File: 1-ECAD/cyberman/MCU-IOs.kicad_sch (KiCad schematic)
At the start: 17 parts, among them U1 ESP32-S3R16V, U15 W25Q128JWPIQ, U16 1054500101, X1 40 MHz

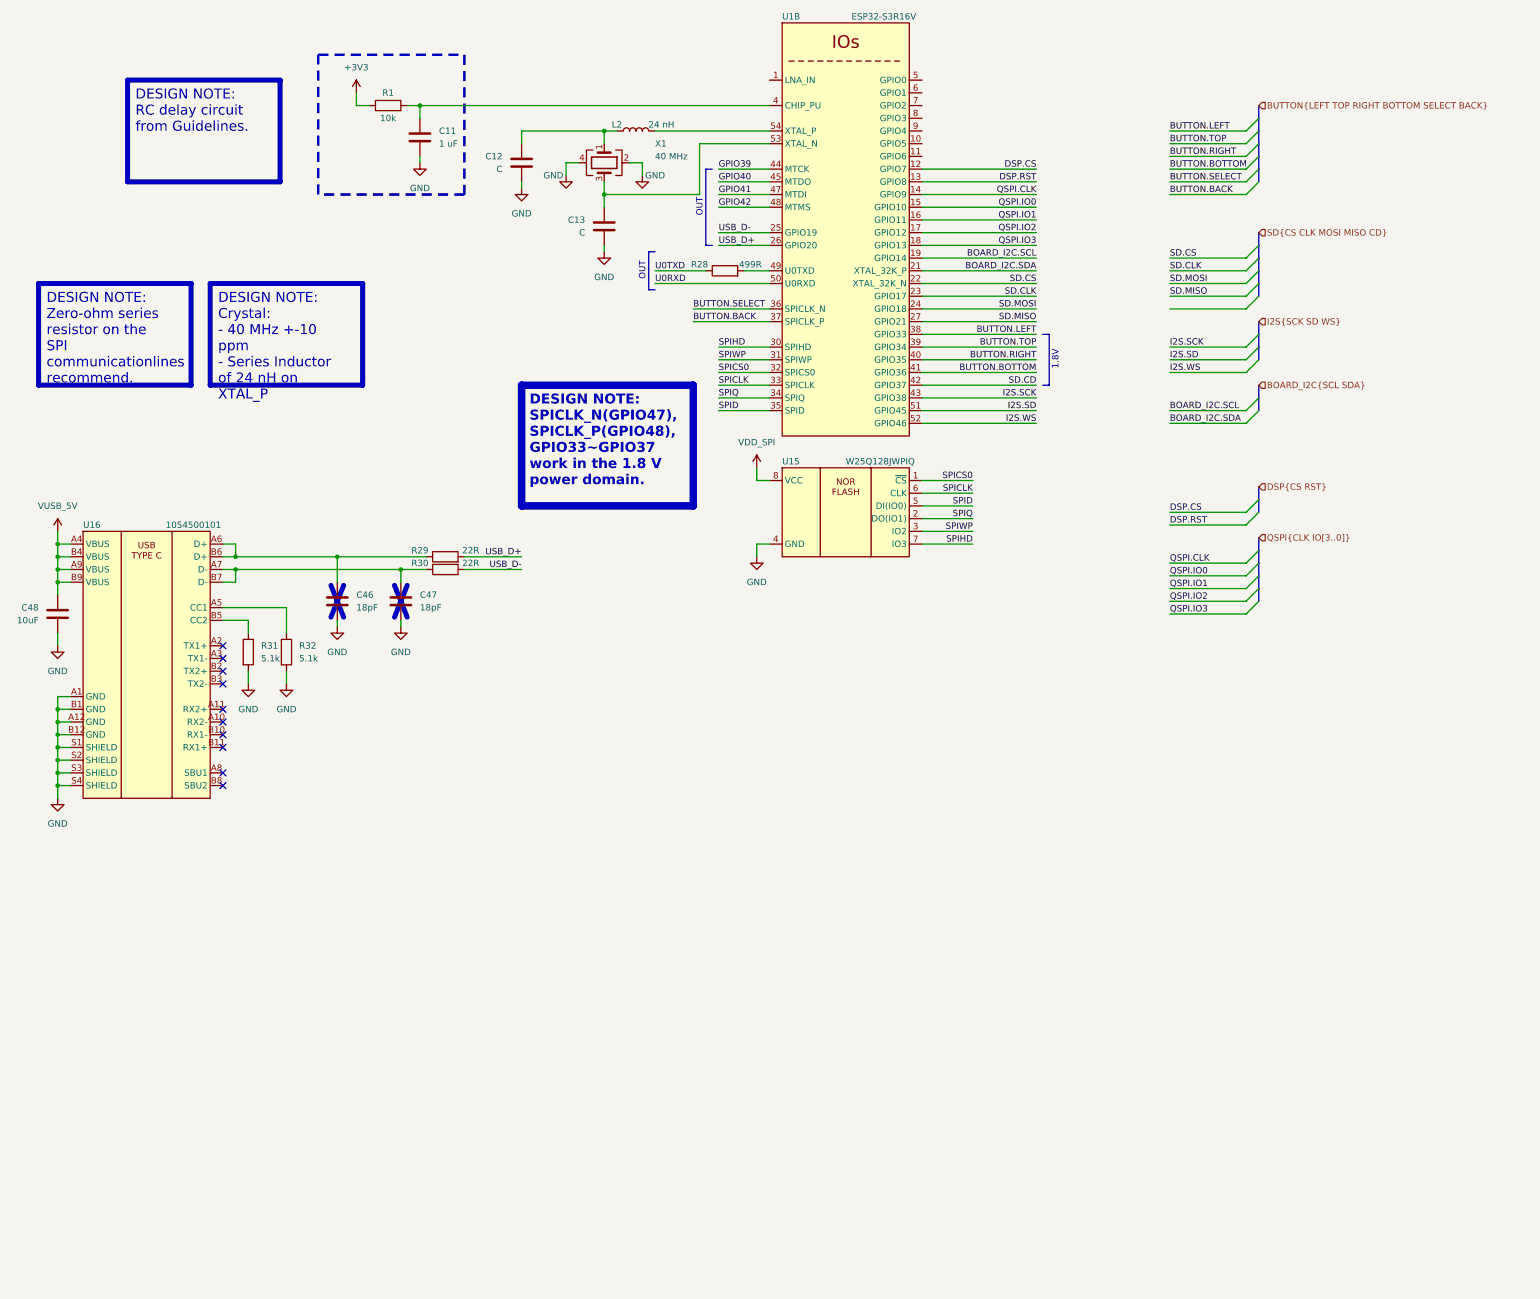
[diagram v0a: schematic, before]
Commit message: add expander io and pic
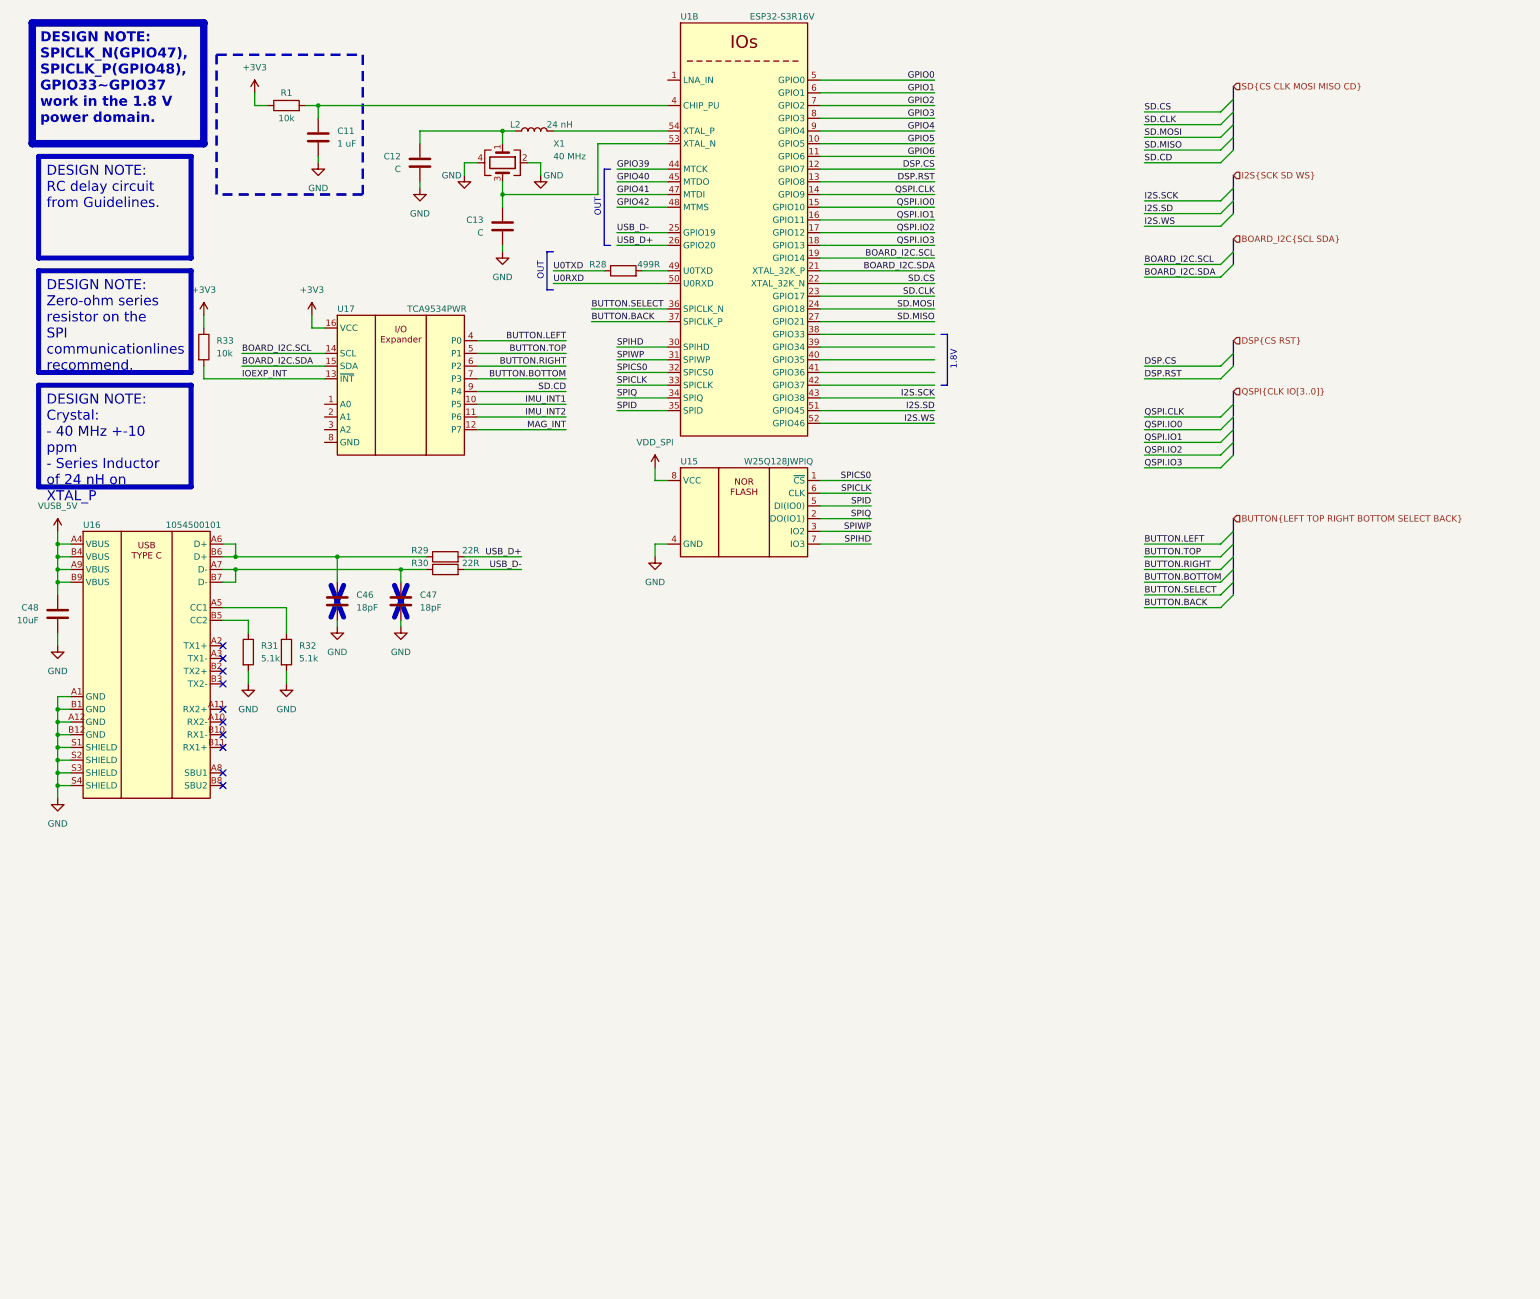
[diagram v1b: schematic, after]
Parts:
- added R33: 10k, symbol Device:R
- added U17: TCA9534PWR, symbol 0_CI_smd:TCA9534PWR
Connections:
- net +3V3: now also R33.1, U17.16 (VCC)
- net BOARD_I2C.SCL: now also U17.14 (SCL)
- net BOARD_I2C.SDA: now also U17.15 (SDA)
- net BUTTON.BOTTOM: now also U17.7 (P3); no longer U1.41 (GPIO36)
- net BUTTON.LEFT: now also U17.4 (P0); no longer U1.38 (GPIO33)
- net BUTTON.RIGHT: now also U17.6 (P2); no longer U1.40 (GPIO35)
- net BUTTON.TOP: now also U17.5 (P1); no longer U1.39 (GPIO34)
- net SD.CD: now also U17.9 (P4); no longer U1.42 (GPIO37)
- net GPIO5: now reaches U1.10 (GPIO5)
- net GPIO6: now reaches U1.11 (GPIO6)
- net GPIO0: now reaches U1.5 (GPIO0)
- net GPIO1: now reaches U1.6 (GPIO1)
- net GPIO2: now reaches U1.7 (GPIO2)
- net GPIO3: now reaches U1.8 (GPIO3)
- net GPIO4: now reaches U1.9 (GPIO4)
- new net IMU_INT1: U17.10 (P5)
- new net IMU_INT2: U17.11 (P6)
- new net IOEXP_INT: R33.2, U17.13 (~{INT})
- new net MAG_INT: U17.12 (P7)
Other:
- moved on the sheet: C11, C12, C13, L2, R1, R28, U15, U1B, X1

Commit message: footpritn day
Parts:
- U1: Supplier 1 PN (none) -> 356-ESP32-S3R16V; Supplier PN 1 356-ESP32-S3R16V -> (none); kode_PN DOTU001 -> (none)
- U15: footprint (none) -> 0_CI_smd:W25Q128JWPIQ
- U16: footprint (none) -> 0_connector_smd:1054500101
- U17: kode PN DOTU015 -> DOTU014

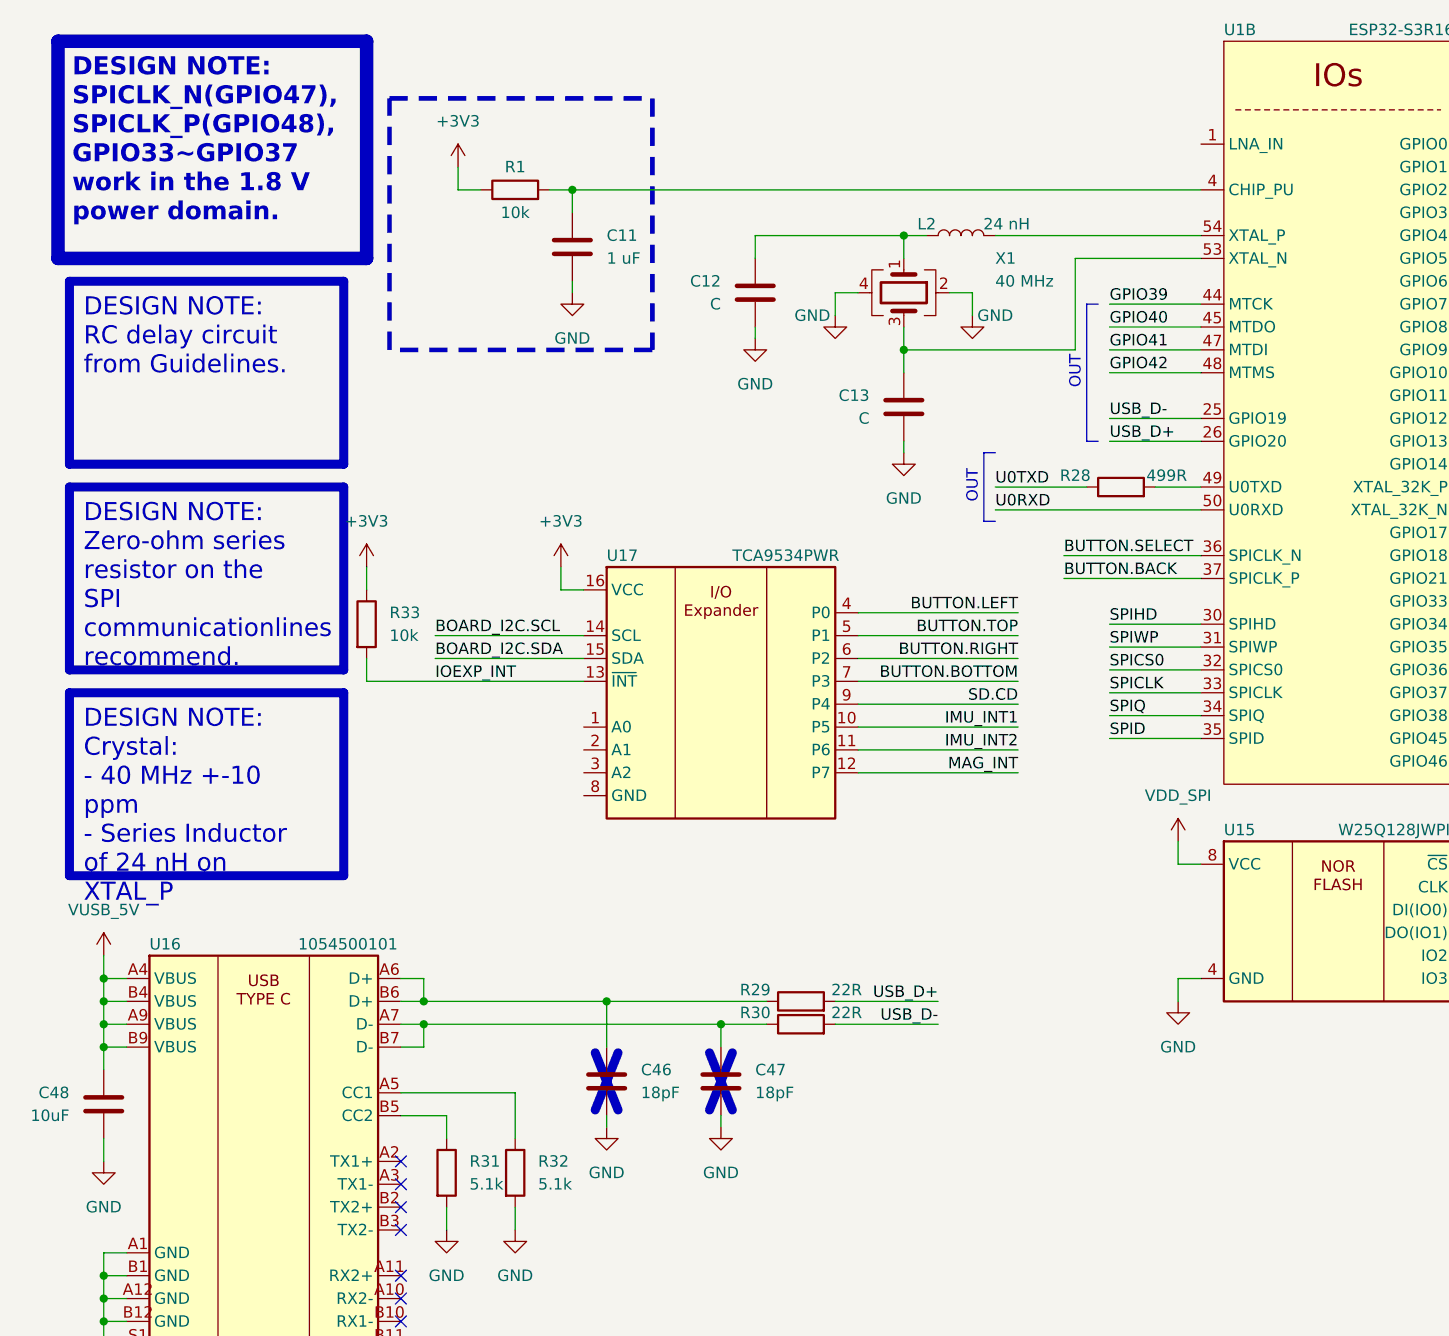
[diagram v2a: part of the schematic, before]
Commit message: new changes
close display page and peripheral schematic
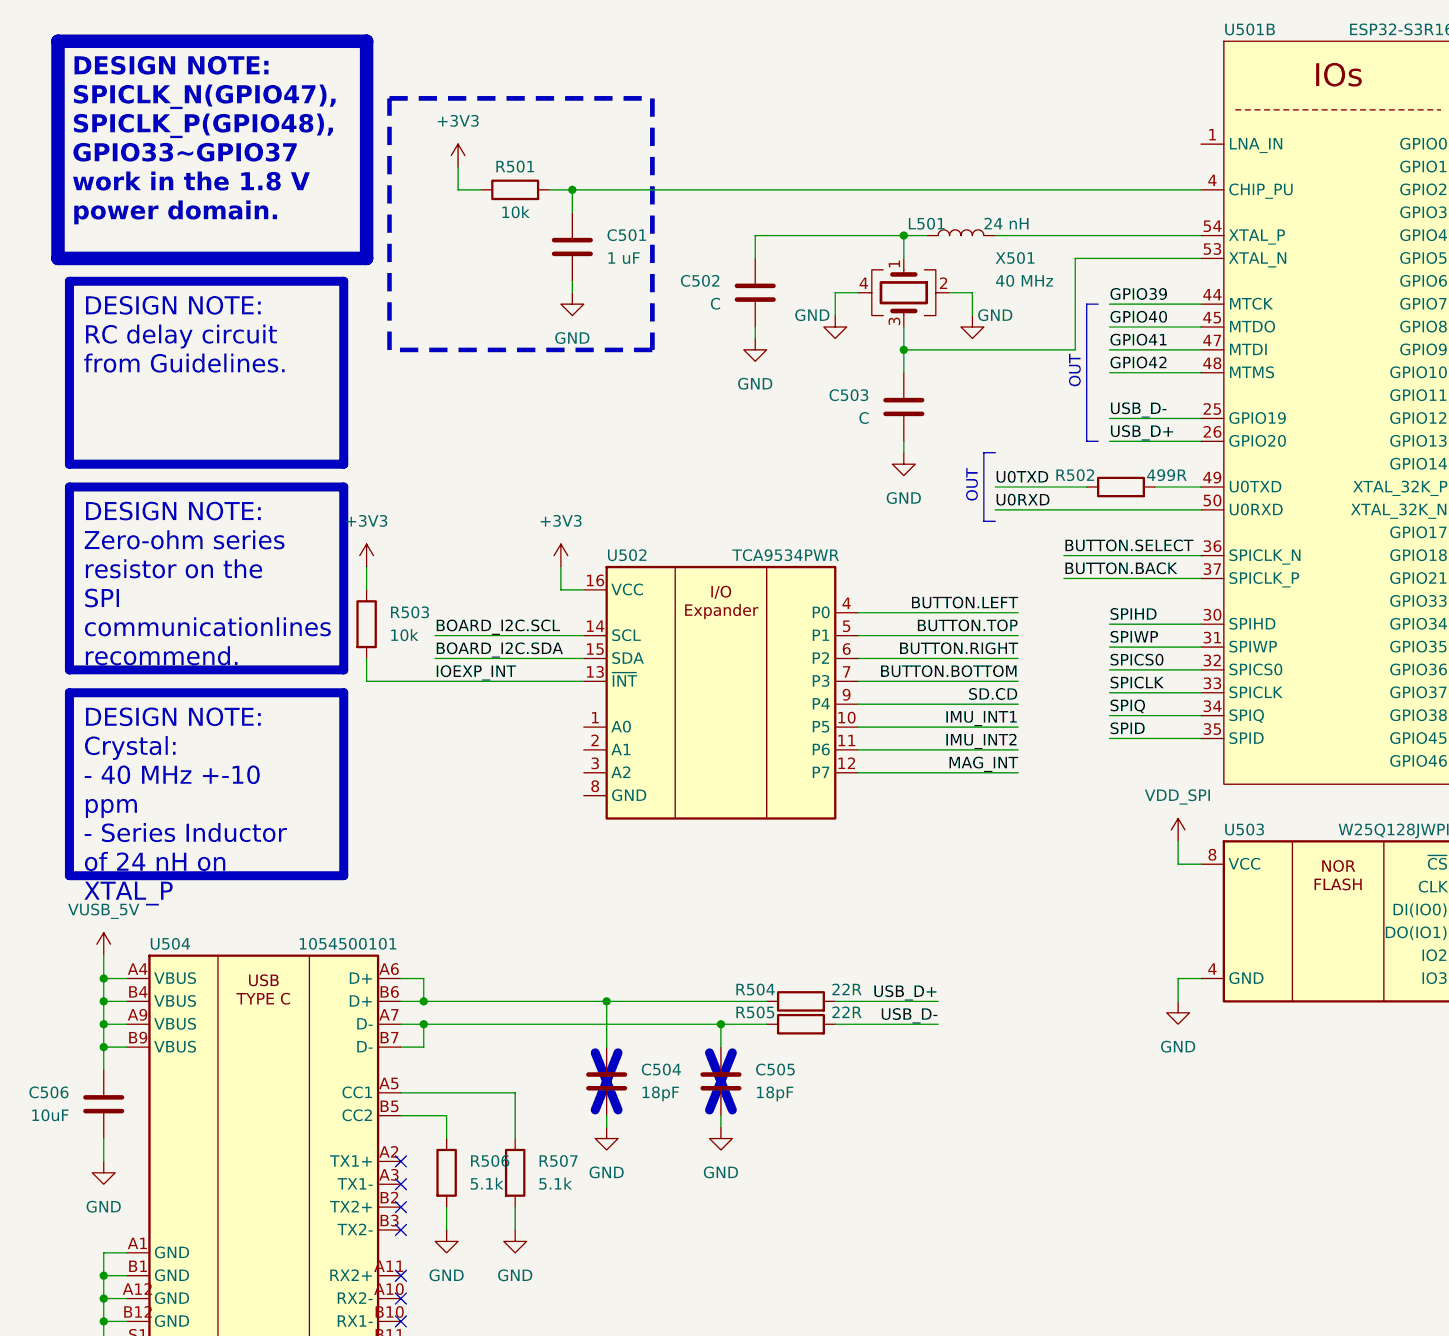
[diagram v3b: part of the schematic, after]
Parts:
- removed U1: ESP32-S3R16V, 0_mcu_espressif:ESP32-S3R16V, symbol 0_mcu_espressif:ESP32-S3
- added U501: ESP32-S3R16V, 0_mcu_espressif:ESP32-S3R16V, symbol 0_mcu_espressif:ESP32-S3
- renumbered C11 to C501, C12 to C502, C13 to C503, C46 to C504, C47 to C505, C48 to C506, L2 to L501, R1 to R501, R28 to R502, R33 to R503, R29 to R504, R30 to R505, R31 to R506, R32 to R507, U17 to U502, U15 to U503, U16 to U504, X1 to X501
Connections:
- net BOARD_I2C.SCL: now also U501.19 (GPIO14)
- net BOARD_I2C.SDA: now also U501.21 (XTAL_32K_P)
- net BUTTON.BACK: now also U501.37 (SPICLK_P)
- net BUTTON.SELECT: now also U501.36 (SPICLK_N)
- net DSP.CS: now also U501.12 (GPIO7)
- net DSP.RST: now also U501.13 (GPIO8)
- net GPIO0: now also U501.5 (GPIO0)
- net GPIO1: now also U501.6 (GPIO1)
- net GPIO2: now also U501.7 (GPIO2)
- net GPIO3: now also U501.8 (GPIO3)
- net GPIO39: now also U501.44 (MTCK)
- net GPIO4: now also U501.9 (GPIO4)
- net GPIO40: now also U501.45 (MTDO)
- net GPIO41: now also U501.47 (MTDI)
- net GPIO42: now also U501.48 (MTMS)
- net GPIO5: now also U501.10 (GPIO5)
- net GPIO6: now also U501.11 (GPIO6)
- net I2S.SCK: now also U501.43 (GPIO38)
- net I2S.SD: now also U501.51 (GPIO45)
- net I2S.WS: now also U501.52 (GPIO46)
- net QSPI.CLK: now also U501.14 (GPIO9)
- net QSPI.IO0: now also U501.15 (GPIO10)
- net QSPI.IO1: now also U501.16 (GPIO11)
- net QSPI.IO2: now also U501.17 (GPIO12)
- net QSPI.IO3: now also U501.18 (GPIO13)
- net SD.CLK: now also U501.23 (GPIO17)
- net SD.CS: now also U501.22 (XTAL_32K_N)
- net SD.MISO: now also U501.27 (GPIO21)
- net SD.MOSI: now also U501.24 (GPIO18)
- net SPICLK: now also U501.33 (SPICLK)
- net SPICS0: now also U501.32 (SPICS0)
- net SPID: now also U501.35 (SPID)
- net SPIHD: now also U501.30 (SPIHD)
- net SPIQ: now also U501.34 (SPIQ)
- net SPIWP: now also U501.31 (SPIWP)
- net U0RXD: now also U501.50 (U0RXD)
- net USB_D+: now also U501.26 (GPIO20)
- net USB_D-: now also U501.25 (GPIO19)
- net at C501.1, R501.2: now also U501.4 (CHIP_PU)
- net at R502.2: now also U501.49 (U0TXD)
- net at C503.1, X501.3: now also U501.53 (XTAL_N)
- net at L501.2: now also U501.54 (XTAL_P)
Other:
- company: (none) -> kode.

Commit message: power page close
siuuuuuuuuuuuu
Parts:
- C501: value 1 uF -> C
- C504, C505: value 18pF -> C
- C506: value 10uF -> C
- L501: value 24 nH -> L
- R501, R503: value 10k -> R
- R502: value 499R -> R
- R504, R505: value 22R -> R
- R506, R507: value 5.1k -> R
- X501: Supplier 1 PN (none) -> C2929402; Supplier PN 1 C2929402 -> (none); kode_PN DOTX001 -> (none)
